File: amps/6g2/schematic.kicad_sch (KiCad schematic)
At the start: 50 parts, among them T1 125P1A, T2 125A10B

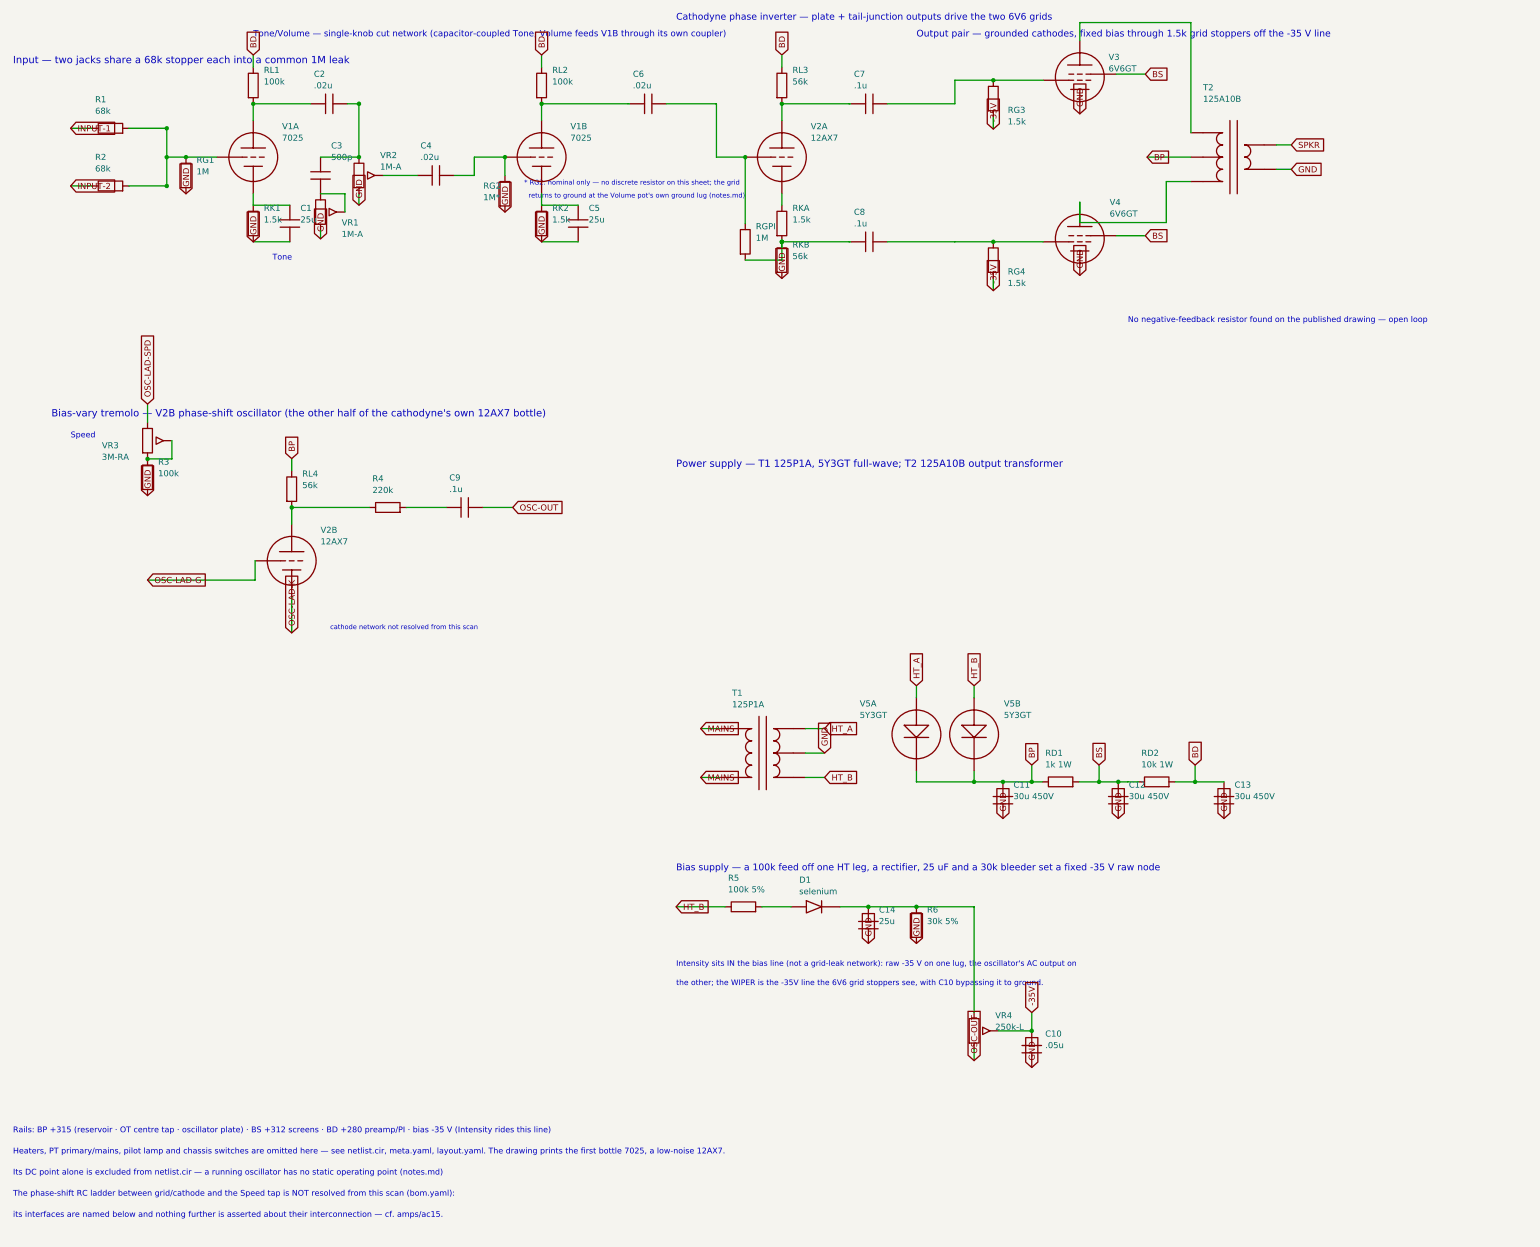
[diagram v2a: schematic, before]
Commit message: Fix: rotated global labels lettered their net names outside the flag
Every global label this pipeline emitted carried (justify left) regardless of
rotation. KiCanvas — like KiCad — draws label text horizontally at 0/180 and
vertically at 90/270 and reads WHICH SIDE of the anchor it letters on from the
justification, so at 180 and 270 the name printed outside an empty flag
outline, struck through by the very wire it names: 219 labels at 180 deg
(including the input-jack flags at top-left of nearly every sheet, the first
glyphs a visitor reads) and 792 GND/rail flags at 270 whose names squeezed at
the flag mouth instead of lettering down the body. The library already
compensated rotation for property text (`pa`); this mirrors that logic for
global labels: justify right at 180/270, left at 0/90.

check_schematics gains the geometry clause whose absence let all 1011
instances through a "no lettering through circuitry" pass: it modelled the
flag box but never the label TEXT, so a name rendered on the wrong side was
invisible to it. The gate now proves justification compensates rotation on
every global label.

Two more things this exposed, fixed in the same engine pass:

- Placement now measures with the renderer's own Newstroke advance table
  (extracted from the vendored kicanvas.js) instead of a flat 0.68-em prose
  average that under-read part lettering by a quarter — the mechanism behind
  every "metered clean, printed through its neighbour" incident. The GATE
  deliberately keeps the coarse ruler: re-ruling it with renderer truth was
  tried and red-flagged 28 of 34 sheets over abutments three visual passes
  had already judged sub-visual (the two-rulers note in schematic_lib.py).
- place_captions' escape ladder runs further, because a banner caption
  measured truly is half again wider than the old estimate believed.

All 34 schematics regenerated; full gate suite green.

🤖 Generated with [Claude Code](https://claude.com/claude-code)

Co-Authored-By: Claude Fable 5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
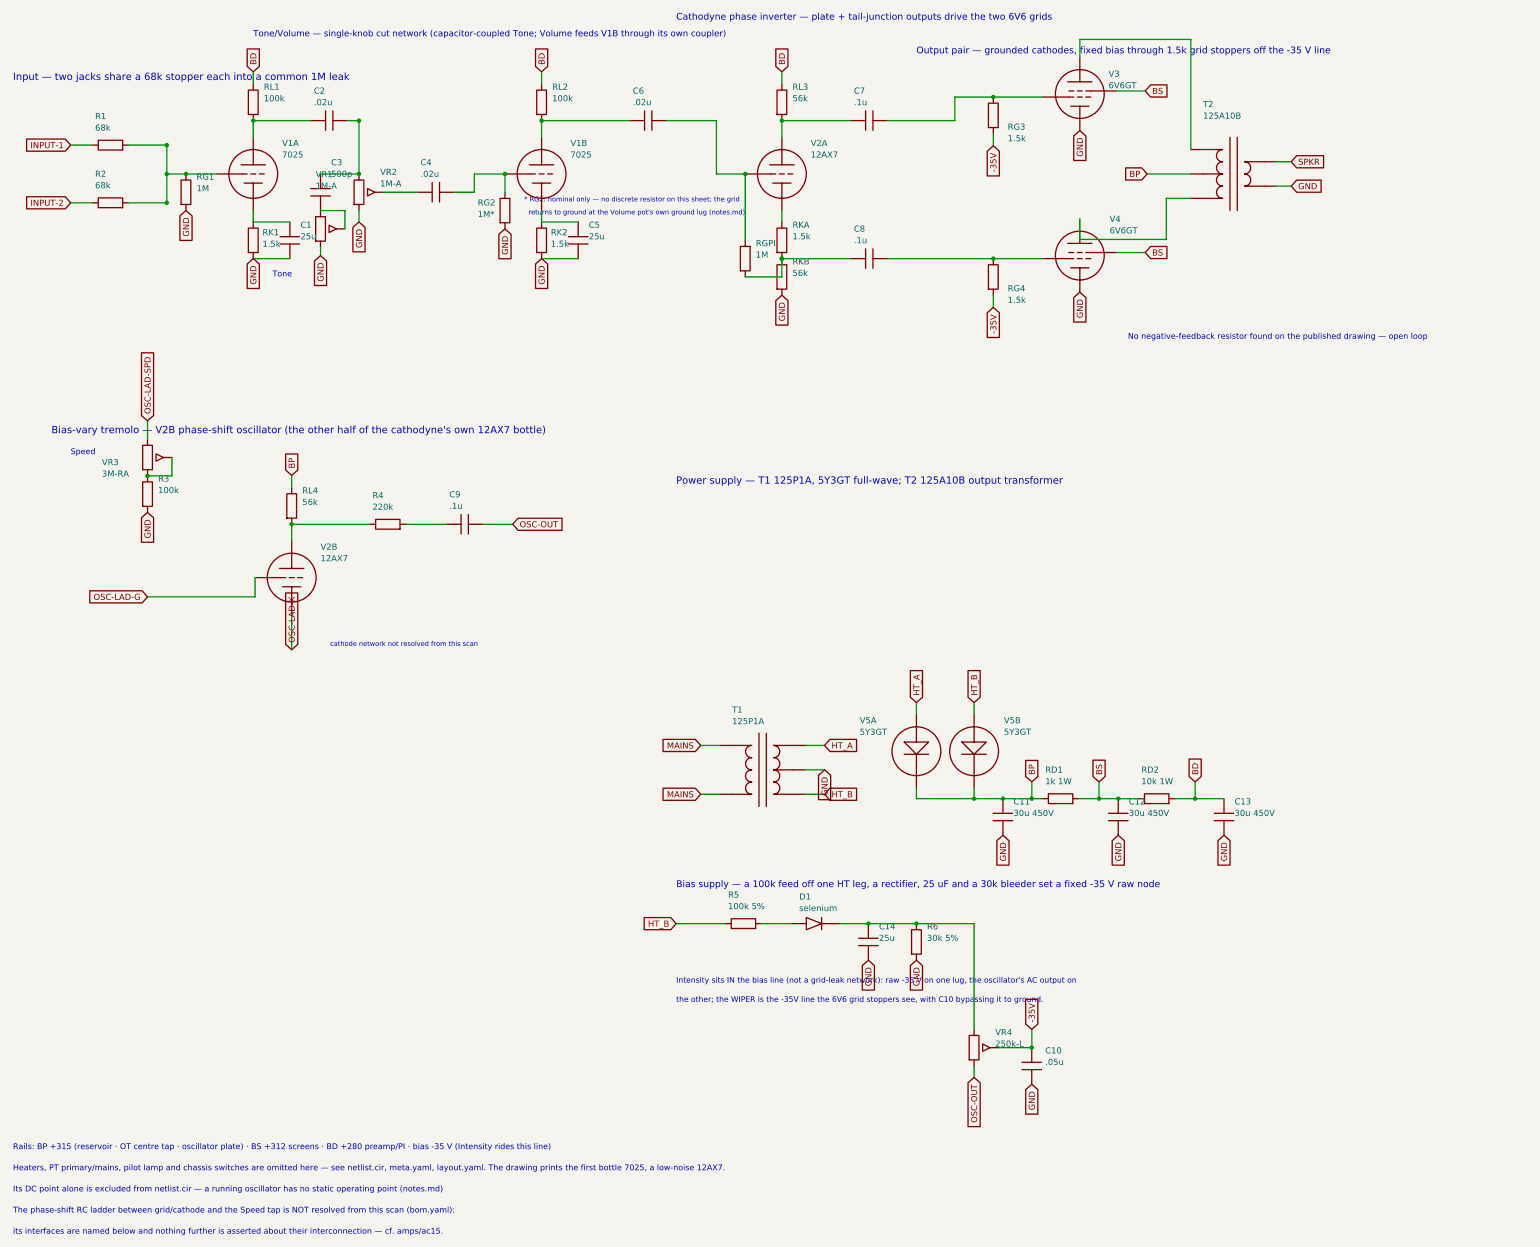
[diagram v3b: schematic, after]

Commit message: Fix: deterministic schematic ids and wires split at every join
- _u() is uuid5 over (amp id, emission order), so a regeneration of an
  unchanged script is byte-identical and a drift gate becomes possible
- write() splits wire segments at symbol pins, wire ends and junction dots,
  so the file connects exactly what the drawing shows under KiCad's
  endpoint-only semantics (270 pins were on a wire's interior; net
  partitions unchanged on all 38 sheets)
- all sheets regenerated; aa864-bassman title block was stale (draft) and
  now matches meta.yaml (verified)

Co-Authored-By: Claude Fable 5.1 <noreply@anthropic.com>
Claude-Session: https://claude.ai/code/session_01KBMfdh37HmCL2iWcBiL5J1
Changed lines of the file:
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@@
   (wire (pts (xy 36.8 52.18) (xy 44.7 52.18))
     (stroke (width 0) (type default)))
-  (wire (pts (xy 44.7 40.18) (xy 44.7 52.18))
+  (wire (pts (xy 44.7 40.18) (xy 44.7 46.18))
+    (stroke (width 0) (type default)))
+  (wire (pts (xy 44.7 46.18) (xy 44.7 52.18))
     (stroke (width 0) (type default)))
   (junction (at 44.7 40.18) (diameter 0) (color 0 0 0 0))
@@
   (wire (pts (xy 194.7 63.8) (xy 208.7 63.8))
     (stroke (width 0) (type default)))
-  (wire (pts (xy 208.7 30.18) (xy 227.08 30.18))
+  (wire (pts (xy 208.7 30.18) (xy 216.7 30.18))
+    (stroke (width 0) (type default)))
+  (wire (pts (xy 216.7 30.18) (xy 227.08 30.18))
     (stroke (width 0) (type default)))
   (symbol (lib_id "cx:PENTODE") (at 234.7 29.545 0) (unit 1)
@@
   (global_label "GND" (shape input) (at 234.7 37.165 270)
     (effects (font (size 1.27 1.27)) (justify right)))
-  (wire (pts (xy 208.7 63.8) (xy 227.08 63.8))
+  (wire (pts (xy 208.7 63.8) (xy 216.7 63.8))
+    (stroke (width 0) (type default)))
+  (wire (pts (xy 216.7 63.8) (xy 227.08 63.8))
     (stroke (width 0) (type default)))
   (symbol (lib_id "cx:PENTODE") (at 234.7 63.165 0) (unit 1)
@@
   (wire (pts (xy 212.7 173.92) (xy 212.7 176.18))
     (stroke (width 0) (type default)))
-  (wire (pts (xy 200.7 176.18) (xy 224.7 176.18))
+  (wire (pts (xy 200.7 176.18) (xy 212.7 176.18))
+    (stroke (width 0) (type default)))
+  (wire (pts (xy 212.7 176.18) (xy 218.7 176.18))
+    (stroke (width 0) (type default)))
+  (wire (pts (xy 218.7 176.18) (xy 224.7 176.18))
     (stroke (width 0) (type default)))
   (junction (at 212.7 176.18) (diameter 0) (color 0 0 0 0))
@@
   (wire (pts (xy 224.7 176.18) (xy 226.89 176.18))
     (stroke (width 0) (type default)))
-  (wire (pts (xy 234.51 176.18) (xy 244.7 176.18))
+  (wire (pts (xy 234.51 176.18) (xy 238.7 176.18))
+    (stroke (width 0) (type default)))
+  (wire (pts (xy 238.7 176.18) (xy 242.7 176.18))
+    (stroke (width 0) (type default)))
+  (wire (pts (xy 242.7 176.18) (xy 244.7 176.18))
     (stroke (width 0) (type default)))
   (junction (at 238.7 176.18) (diameter 0) (color 0 0 0 0))
@@
   (wire (pts (xy 244.7 176.18) (xy 246.89 176.18))
     (stroke (width 0) (type default)))
-  (wire (pts (xy 254.51 176.18) (xy 264.7 176.18))
+  (wire (pts (xy 254.51 176.18) (xy 258.7 176.18))
+    (stroke (width 0) (type default)))
+  (wire (pts (xy 258.7 176.18) (xy 264.7 176.18))
     (stroke (width 0) (type default)))
   (junction (at 258.7 176.18) (diameter 0) (color 0 0 0 0))

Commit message: Add: real tube pin numbers and readable valve glyphs on every schematic
Phase B of the drawing program. A factory service sheet numbers every tube
pin, because the number is what a technician puts a probe on. This corpus
printed none, and the numbers hidden in its symbols were positional
placeholders (P=1, G=2, K=3) that would have published a 6V6GT's plate as
pin 1 when it is pin 3.

1055 electrodes now carry the real number, 1027 lettered (27 are shared
filaments deduped, 1 dropped for want of clear space on the 6G2). Resolved per
instance from reference/tubes/<slug>.yaml through the same alias resolution the
layout renderer uses, so a 12AX7 section and a 6SL7 section each get their own
basing. A valve whose basing the corpus does not carry prints nothing rather
than a wrong number.

Section letters and basing units are now separate things, which cost a detour
worth recording. The RCA 12AX7-A sheet reads "Pin 1 - Plate of Unit No.2 ...
Pin 6 - Plate of Unit No.1", so unit numbering is not pin order; the 5Y3 and
GZ34 number their units in opposite pin order, so nothing positional can
express it. But the section LETTER is a designator, not a basing fact: this
corpus, like every technician, calls the first stage in signal order V1A, and
five amps' prose already did. On four amps the factory sheets put that first
stage on the other half -- the AA764's own schematic prints +200 V on pin 1 --
so those drawings now state their unit explicitly, each citing its source, and
no letter, netlist, parts list or layout comment changed. 183 layout comments
agree with the printed numbers, 0 disagree. A guard fires if two halves of one
bottle resolve to the same unit, which is exactly how this was found.

Glyphs: the cathode gains a bracket and filament hairpin so it can no longer be
confused with the plate bar, the pentode's screen sits on its own row, and a
rectifier draws as one envelope over its sections instead of two apparent
bottles. Line weights are scaled per sheet to a co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
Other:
- note added: "1"
- note added: "2"
- note added: "2,8"
- note added: "3"
- note added: "4"
- note added: "5"
- note added: "6"
- note added: "7"
- note added: "8"
